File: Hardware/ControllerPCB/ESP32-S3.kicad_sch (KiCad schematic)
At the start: 55 parts, among them J1 UJ20-C-H-G-SMT-1-P16-TR, J4 54602-908LF, J5 Conn_TagConnect_TC2030-NL_ESP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, J8 104031-0811, SW1 SW_Push, SW2 SW_Push, U1 ESP32-S3-WROOM-1, U7 AP7333-33SRG-7

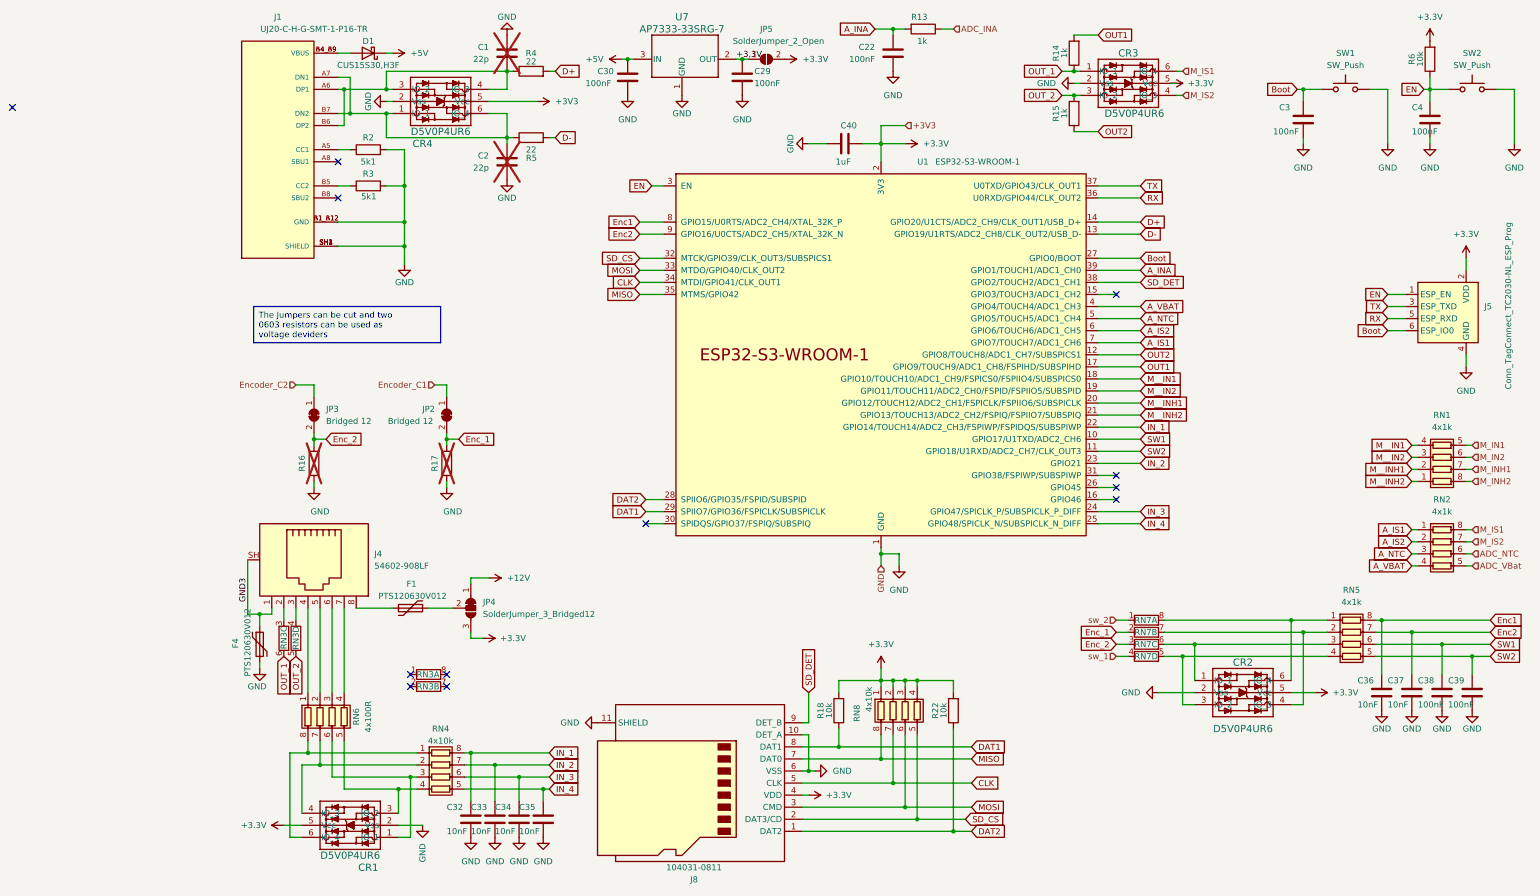
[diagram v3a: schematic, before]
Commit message: fix schematics and pins for the encoder
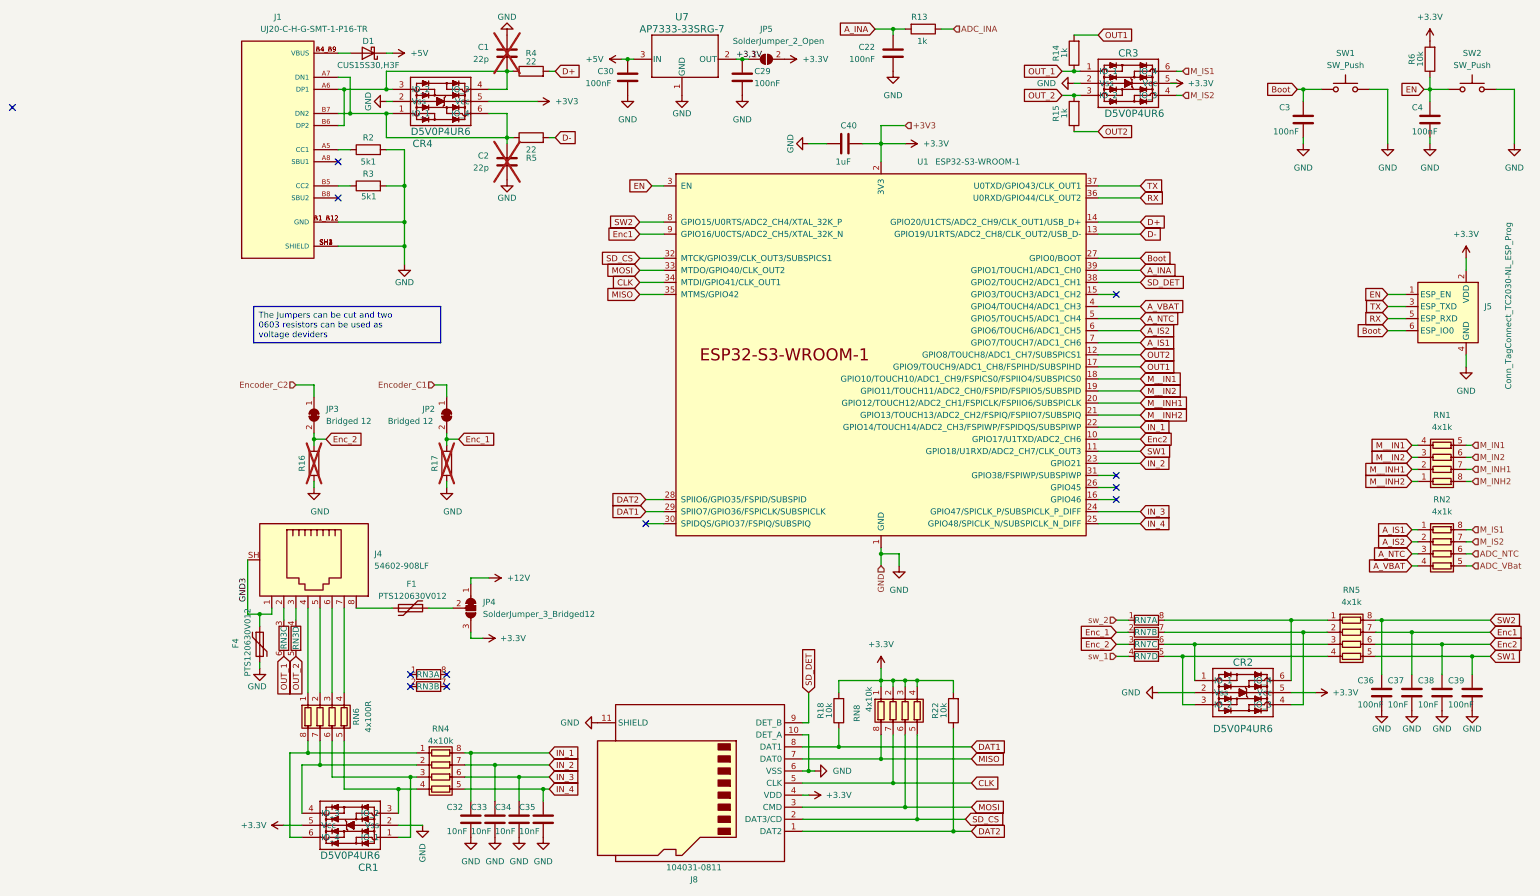
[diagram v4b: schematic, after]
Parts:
- C1, C2, C22, C29, C3, C30, C32, C33, C34, C35, C37, C39: footprint Capacitor_SMD:C_0603_1608Metric -> BugWiper_lib:C_0603_1608Metric
- C36: value 10nF -> 100nF; footprint Capacitor_SMD:C_0603_1608Metric -> BugWiper_lib:C_0603_1608Metric
- C38: value 100nF -> 10nF; footprint Capacitor_SMD:C_0603_1608Metric -> BugWiper_lib:C_0603_1608Metric
- C40: footprint Capacitor_SMD:C_0805_2012Metric -> BugWiper_lib:C_0805_2012Metric
- D1: footprint Diode_SMD:D_SOD-323_HandSoldering -> BugWiper_lib:D_SOD-323_HandSoldering
- F1, F4: footprint Resistor_SMD:R_1206_3216Metric -> BugWiper_lib:R_1206_3216Metric
- R13, R14, R15, R16, R17, R18, R2, R22, R3, R4, R5, R6: footprint Resistor_SMD:R_0603_1608Metric -> BugWiper_lib:R_0603_1608Metric
- U7: footprint SOT23R_DIO -> BugWiper_lib:SOT23R_DIO
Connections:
- net Enc1: now also C37.1, RN5.7 (R2.2), U1.9 (GPIO16/U0CTS/ADC2_CH5/XTAL_32K_N); no longer C36.1, RN5.8 (R1.2), U1.8 (GPIO15/U0RTS/ADC2_CH4/XTAL_32K_P)
- net Enc2: now also C38.1, RN5.6 (R3.2), U1.10 (GPIO17/U1TXD/ADC2_CH6); no longer C37.1, RN5.7 (R2.2), U1.9 (GPIO16/U0CTS/ADC2_CH5/XTAL_32K_N)
- net SW1: now also C39.1, RN5.5 (R4.2), U1.11 (GPIO18/U1RXD/ADC2_CH7/CLK_OUT3); no longer C38.1, RN5.6 (R3.2), U1.10 (GPIO17/U1TXD/ADC2_CH6)
- net SW2: now also C36.1, RN5.8 (R1.2), U1.8 (GPIO15/U0RTS/ADC2_CH4/XTAL_32K_P); no longer C39.1, RN5.5 (R4.2), U1.11 (GPIO18/U1RXD/ADC2_CH7/CLK_OUT3)

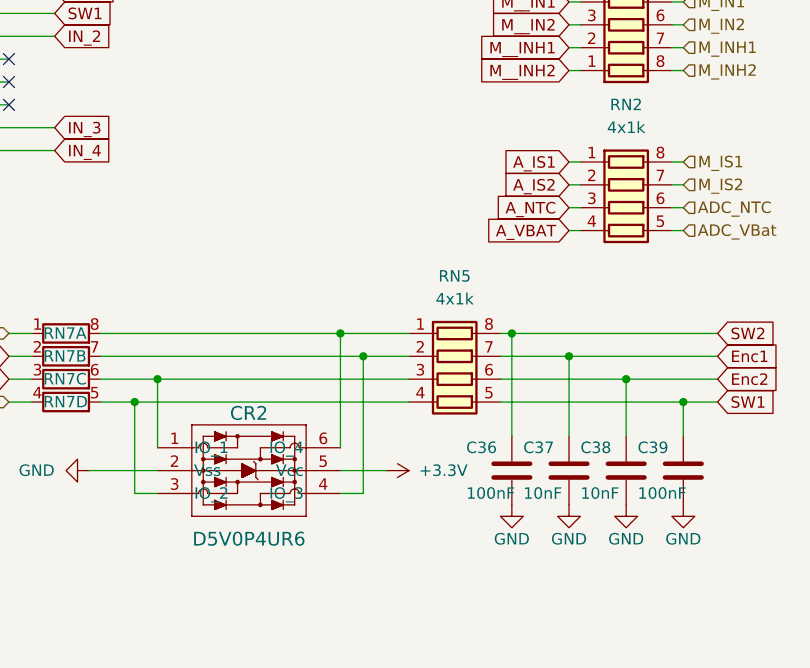
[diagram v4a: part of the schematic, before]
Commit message: update controller PCB: change Encoder filter to 1nF add 0 Ohm resistor for JP1 to BOM
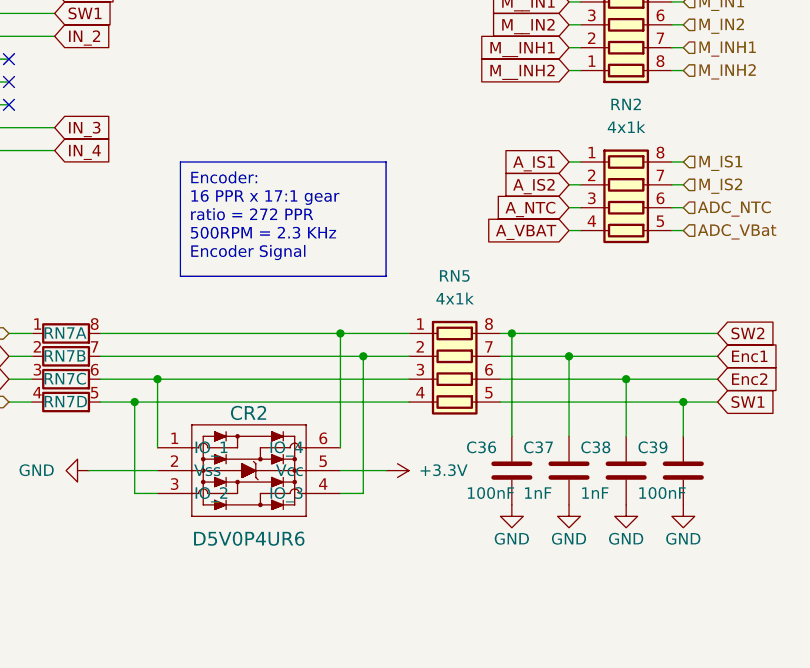
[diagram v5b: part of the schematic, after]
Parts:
- C37, C38: value 10nF -> 1nF
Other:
- company: (none) -> M. Scholjegerdes
- title: (none) -> BugWiper 2.0 Controller PCB
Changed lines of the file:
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@@
 (kicad_sch (version 20230121) (generator eeschema)
   (paper "A4")
+  (title_block
+    (title "BugWiper 2.0 Controller PCB")
+    (date "2025-06-02")
+    (rev "V1.1")
+    (company "M. Scholjegerdes")
+  )
   (junction (at 212.09 148.59) (diameter 0) (color 0 0 0 0)
   )
@@
     (stroke (width 0) (type default))
   )
+  (text_box "Encoder:\n16 PPR x 17:1 gear ratio = 272 PPR\n500RPM = 2.3 KHz Encoder Signal"
+    (at 217.17 121.92 0) (size 22.86 12.7)
+    (stroke (width 0) (type default))
+    (fill (type none))
+    (effects (font (size 1.27 1.27)) (justify left top))
+  )
   (text_box "The Jumpers can be cut and two 0603 resistors can be used as voltage deviders"
     (at 16.51 74.93 0) (size 39.37 7.62)
@@
       (effects (font (size 1.27 1.27)) (justify left))
     )
-    (property "Value" "10nF" (at 255.27 158.75 0)
+    (property "Value" "1nF" (at 255.27 158.75 0)
       (effects (font (size 1.27 1.27)) (justify left))
     )
@@
       (effects (font (size 1.27 1.27)) (justify left))
     )
-    (property "Value" "10nF" (at 261.62 158.75 0)
+    (property "Value" "1nF" (at 261.62 158.75 0)
       (effects (font (size 1.27 1.27)) (justify left))
     )

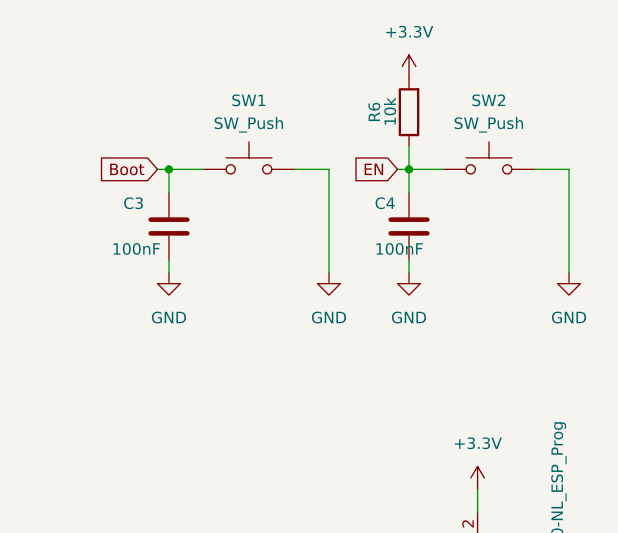
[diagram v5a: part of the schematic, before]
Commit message: Update PCB files and documentation for BugWiper 2.0: change revision to V1.2, update value from C4 from 100nF to 470nF
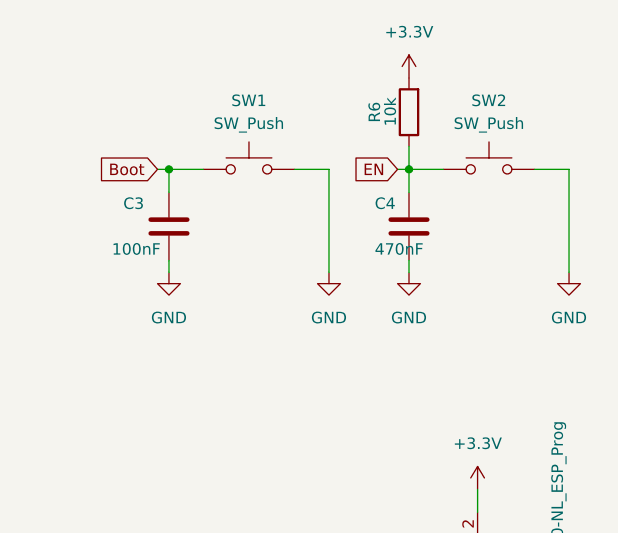
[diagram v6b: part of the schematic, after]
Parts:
- C4: value 100nF -> 470nF; Manufacturer_Part_Number CL10B104KB8NNNC -> CL10B474KA8NFNC; Mouser Part Number 187-CL10B104KB8NNNC -> 187-CL10B474KA8NFNC
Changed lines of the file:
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@@
   (title_block
     (title "BugWiper 2.0 Controller PCB")
-    (date "2025-06-02")
-    (rev "V1.1")
+    (date "2026-05-04")
+    (rev "V1.2")
     (company "M. Scholjegerdes")
   )
@@
       (effects (font (size 1.27 1.27)) (justify left))
     )
-    (property "Value" "100nF" (at 260.35 38.1 0)
+    (property "Value" "470nF" (at 260.35 38.1 0)
       (effects (font (size 1.27 1.27)) (justify left))
     )
@@
       (effects (font (size 1.27 1.27)) hide)
     )
-    (property "Description" "100nF+/-10% 50V X7R 0603" (at 264.16 35.56 0)
+    (property "Description" "470nF+/-10% 25V X7R 0603" (at 264.16 35.56 0)
       (effects (font (size 1.27 1.27)) hide)
     )
@@
       (effects (font (size 1.27 1.27)) hide)
     )
-    (property "Manufacturer_Part_Number" "CL10B104KB8NNNC" (at 264.16 35.56 0)
+    (property "Manufacturer_Part_Number" "CL10B474KA8NFNC" (at 264.16 35.56 0)
       (effects (font (size 1.27 1.27)) hide)
     )
-    (property "Mouser Part Number" "187-CL10B104KB8NNNC" (at 264.16 35.56 0)
+    (property "Mouser Part Number" "187-CL10B474KA8NFNC" (at 264.16 35.56 0)
       (effects (font (size 1.27 1.27)) hide)
     )
